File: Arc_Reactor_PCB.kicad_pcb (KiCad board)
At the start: 4 copper layers, 70 x 70 mm, 42 parts, among them J1 Conn_01x01, J2 Conn_01x01, J3 USB_C_Receptacle, J4 Conn_01x03, SW1 SW_Push, SW2 SW_Push, U1 ESP32-C3-MINI-1, U2 AP63205WU, U3 SN74AHCT1G125, U4 LM66200DRLR, U5 AP2112K-3.3

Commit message: Updates for production
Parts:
- C10, C3, C9: footprint Capacitor_SMD:C_0402_1005Metric -> Capacitor_SMD:C_0603_1608Metric
- L1: footprint SWPA4030S4R7MT:IND-SMD_L4.0-W4.0 -> FNR4030S4R7MT:IND-SMD_L4.0-W4.0_FNR40XXS
- moved D1 2.23 mm to (103.0, 117.9)
- moved C7 2.07 mm to (97.2, 117.3), turned to 0 degrees
- moved C10 0.61 mm to (90.1, 94.3)
- moved C9 0.58 mm to (84.1, 94.2)
- moved C3 0.51 mm to (95.5, 95.1)
- moved L1 0.10 mm to (105.5, 113.6)
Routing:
- net BUCK_5V: track 26.5 -> 22.4 mm
- net GND: track 13.0 -> 14.1 mm
- net +3V3: track 14.0 -> 13.0 mm, vias 7 -> 6
- added copper zone on F.Cu, net BUCK_5V
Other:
- board text added: "ARC Reactor PCB Rev. A"
- board text removed: "ARC Reactor PCB"

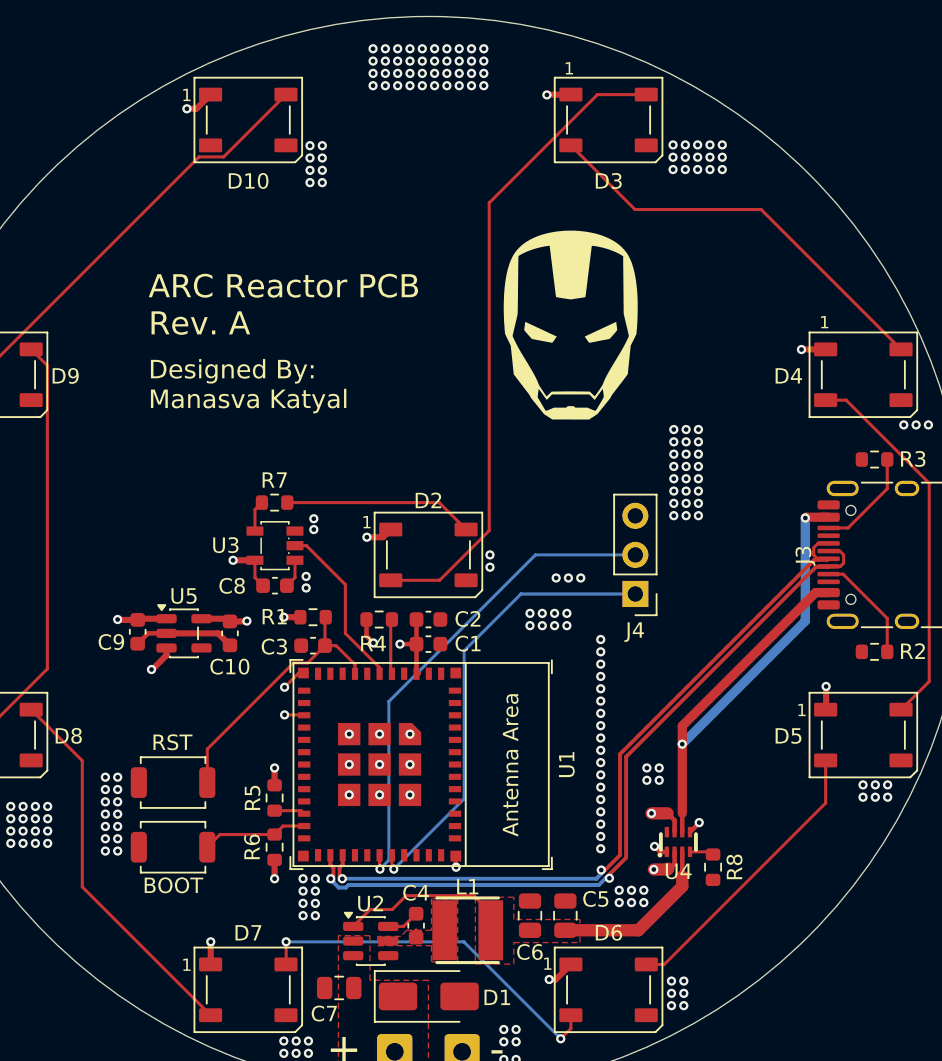
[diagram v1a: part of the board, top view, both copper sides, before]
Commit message: Improve placement/routing
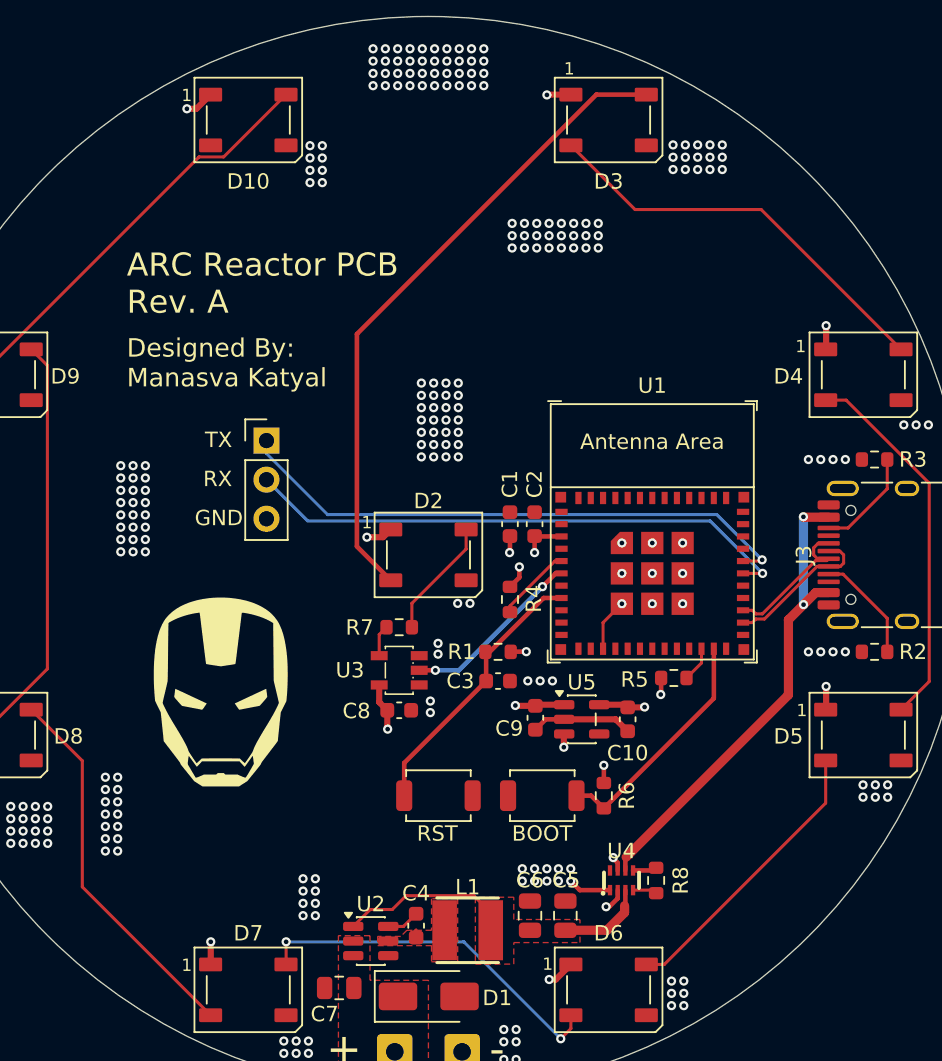
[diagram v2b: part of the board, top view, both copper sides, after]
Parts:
- removed G2: LOGO, LOGO
- moved G1 33.0 mm to (89.5, 98.1)
- moved R5 27.1 mm to (119.0, 97.2), turned to 0 degrees
- moved C10 26.4 mm to (116.0, 99.9)
- moved C9 26.4 mm to (110.0, 99.8)
- moved U5 26.4 mm to (113.0, 99.9)
- moved J4 26.0 mm to (92.5, 81.8), turned to 0 degrees
- moved SW2 24.2 mm to (110.4, 104.8)
- moved R6 21.7 mm to (114.4, 104.8), turned to -90 degrees
- moved U1 21.3 mm to (117.5, 87.7), turned to 0 degrees
- moved SW1 17.3 mm to (103.7, 104.8), turned to 180 degrees
- moved C3 12.2 mm to (107.5, 97.4), turned to 180 degrees
- moved R1 12.2 mm to (107.5, 95.5), turned to 180 degrees
- moved R7 11.5 mm to (101.1, 93.9)
- moved U3 11.4 mm to (101.1, 96.7)
- moved C8 11.4 mm to (101.1, 99.3)
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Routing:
- net /MCU_USB_D-: track 49.6 -> 9.75 mm, vias 2 -> 0
- net /MCU_USB_D+: track 48.5 -> 9.78 mm, vias 2 -> 0
- net /BOOT: track 6.87 -> 15.5 mm
- net USB_5V: track 39.6 -> 31.4 mm
- net /MCU_UART_TX: track 29.7 -> 37.2 mm
- net BUCK_5V: track 22.4 -> 17.2 mm
- net Net-(D2-DIN): track 12.3 -> 7.81 mm
- net /MCU_UART_RX: track 32.0 -> 36.0 mm
- net +5V: track 28.3 -> 24.9 mm
- net +3V3: track 13.0 -> 11.5 mm, vias 6 -> 7
- net Net-(U1-GPIO2/ADC1_CH2): track 3.59 -> 4.96 mm
- net /MCU_LED_DATA: track 11.0 -> 11.9 mm, vias 0 -> 2
- net GND: track 14.1 -> 14.6 mm, vias 253 -> 282
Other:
- board text added: "GND"
- board text added: "RX"
- board text added: "TX"

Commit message: Add SMAJ5.0A TVS on USB VBUS
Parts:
- added D2: SMAJ5.0A, Diode_SMD:D_SMA, F.Cu at (122.8, 104.2)
- renumbered D9 to D10, D10 to D11, D2 to D3, D3 to D4, D4 to D5, D5 to D6, D6 to D7, D7 to D8, D8 to D9
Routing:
- net /LED3_DOUT: track 18.8 -> 20.1 mm
- net GND: vias 282 -> 288

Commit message: Update Back Silkscreen with Arc Reactor SVG
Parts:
- added G2: LOGO, LOGO, B.Cu at (103.0, 89.2)

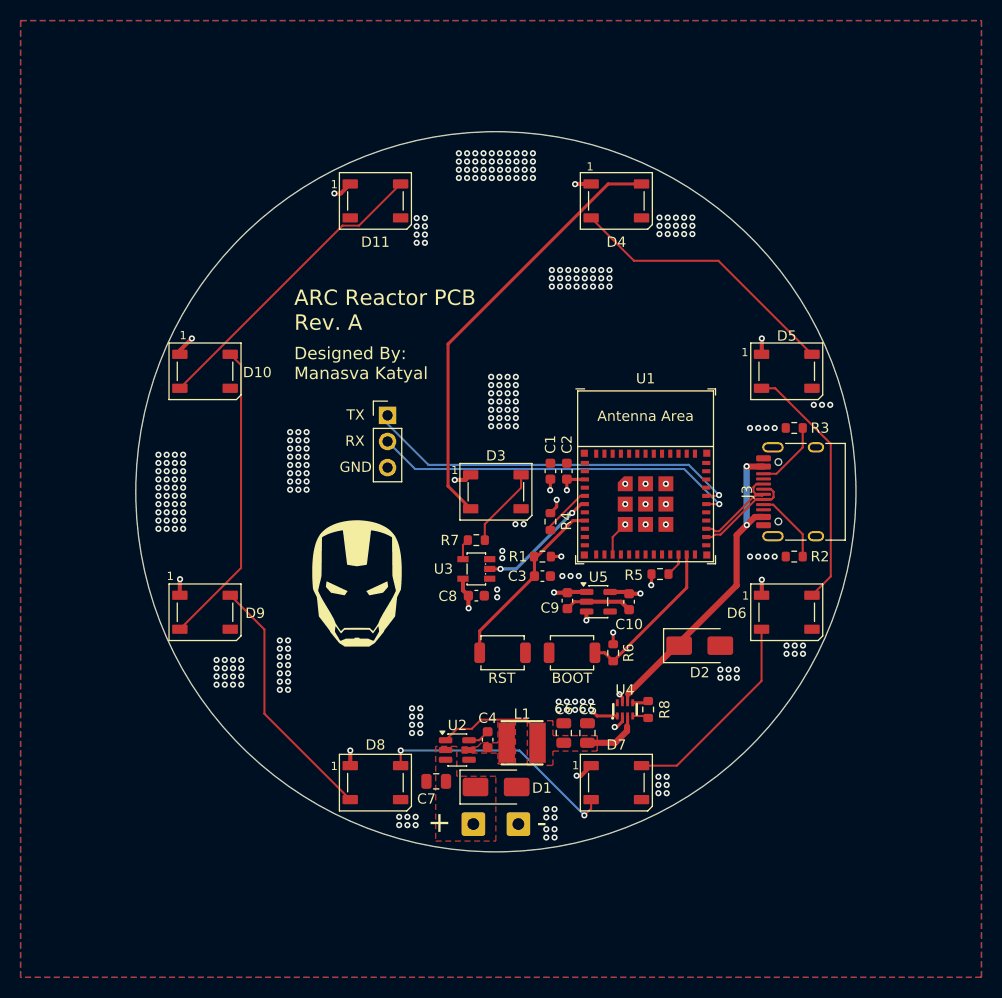
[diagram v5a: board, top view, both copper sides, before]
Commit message: Trim board edge flat at USB-C
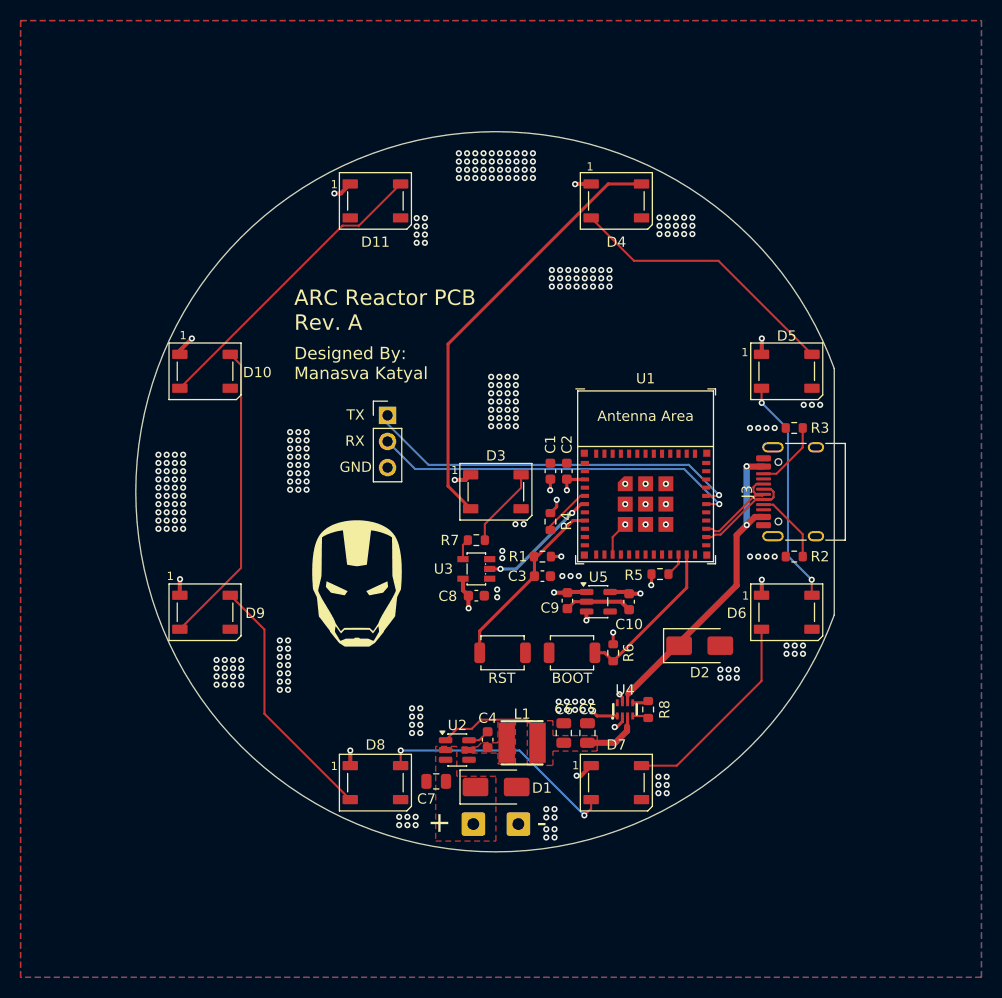
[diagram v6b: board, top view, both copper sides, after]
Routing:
- net /LED2_DOUT: track 24.4 -> 22.1 mm, vias 0 -> 2
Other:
- board size 70 x 70 mm -> 67.9 x 70 mm
